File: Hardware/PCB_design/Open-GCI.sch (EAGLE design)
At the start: 29 parts, among them IC1 IC1, IC2 IC2, X1 USB

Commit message: Updated the schematics
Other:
- note added: "1.0"
- note added: "https://github.com/milador/Open-GCI"
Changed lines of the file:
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@@
 <part name="P+9" library="supply2" library_urn="urn:adsk.eagle:library:372" deviceset="+5V/2" device=""/>
 <part name="JP1" library="pinhead" library_urn="urn:adsk.eagle:library:325" deviceset="PINHD-1X2" device="" package3d_urn="urn:adsk.eagle:package:22435/2" value="No Rpi"/>
+<part name="FRAME1" library="frames" library_urn="urn:adsk.eagle:library:229" deviceset="FRAME_C_L" device="" value="https://github.com/milador/Open-GCI"/>
 </parts>
 <sheets>
 <sheet>
 <plain>
+<text x="270.51" y="-149.86" size="2.54" layer="94">https://github.com/milador/Open-GCI</text>
+<text x="360.68" y="-149.86" size="2.54" layer="94">1.0</text>
 </plain>
 <instances>
@@
 <instance part="P+9" gate="G$1" x="196.85" y="36.83"/>
 <instance part="JP1" gate="G$1" x="186.69" y="22.86" rot="R270"/>
+<instance part="FRAME1" gate="G$1" x="-184.15" y="-157.48" smashed="yes"/>
+<instance part="FRAME1" gate="G$2" x="267.97" y="-157.48"/>
 </instances>
 <busses>

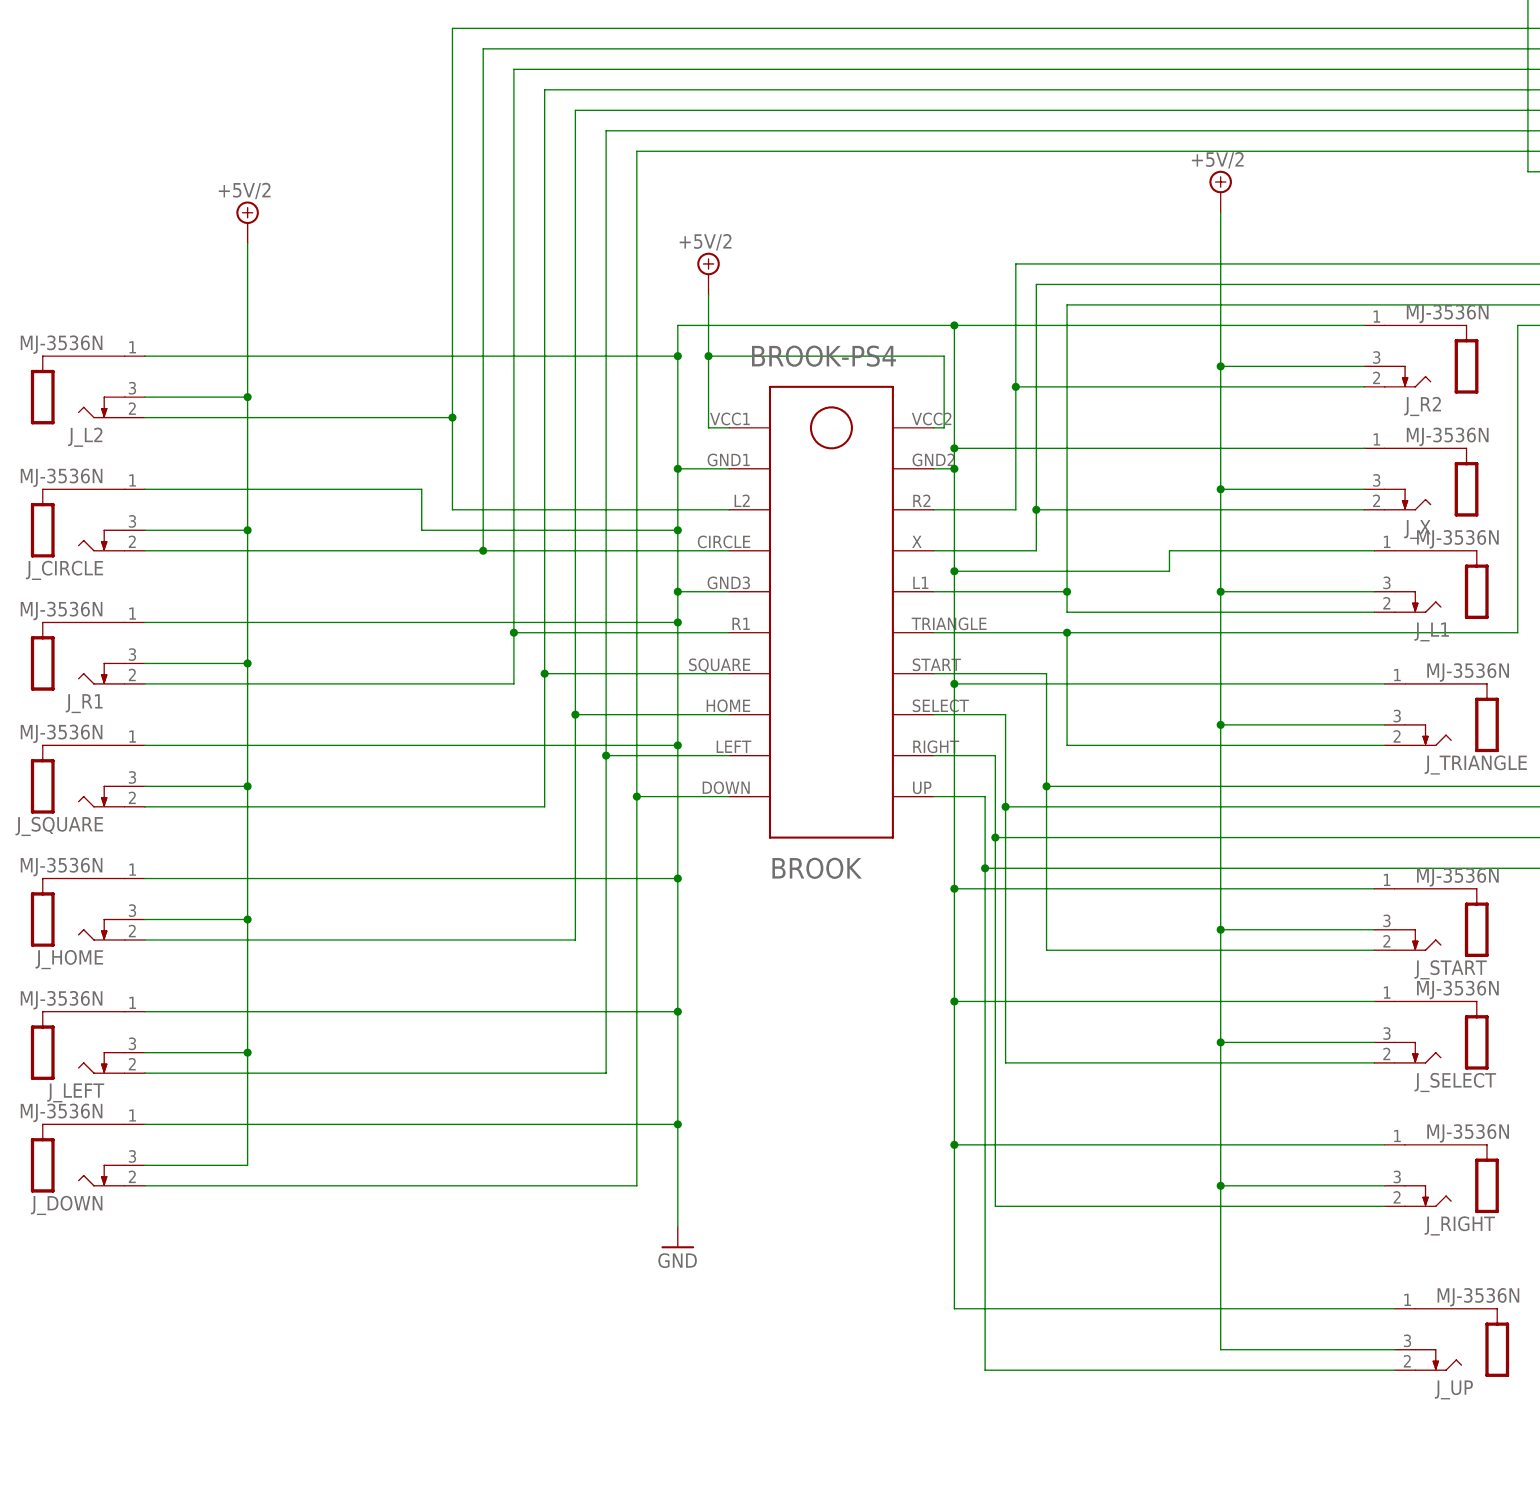
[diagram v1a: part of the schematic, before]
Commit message: Fixed the 3.5mm jack issue
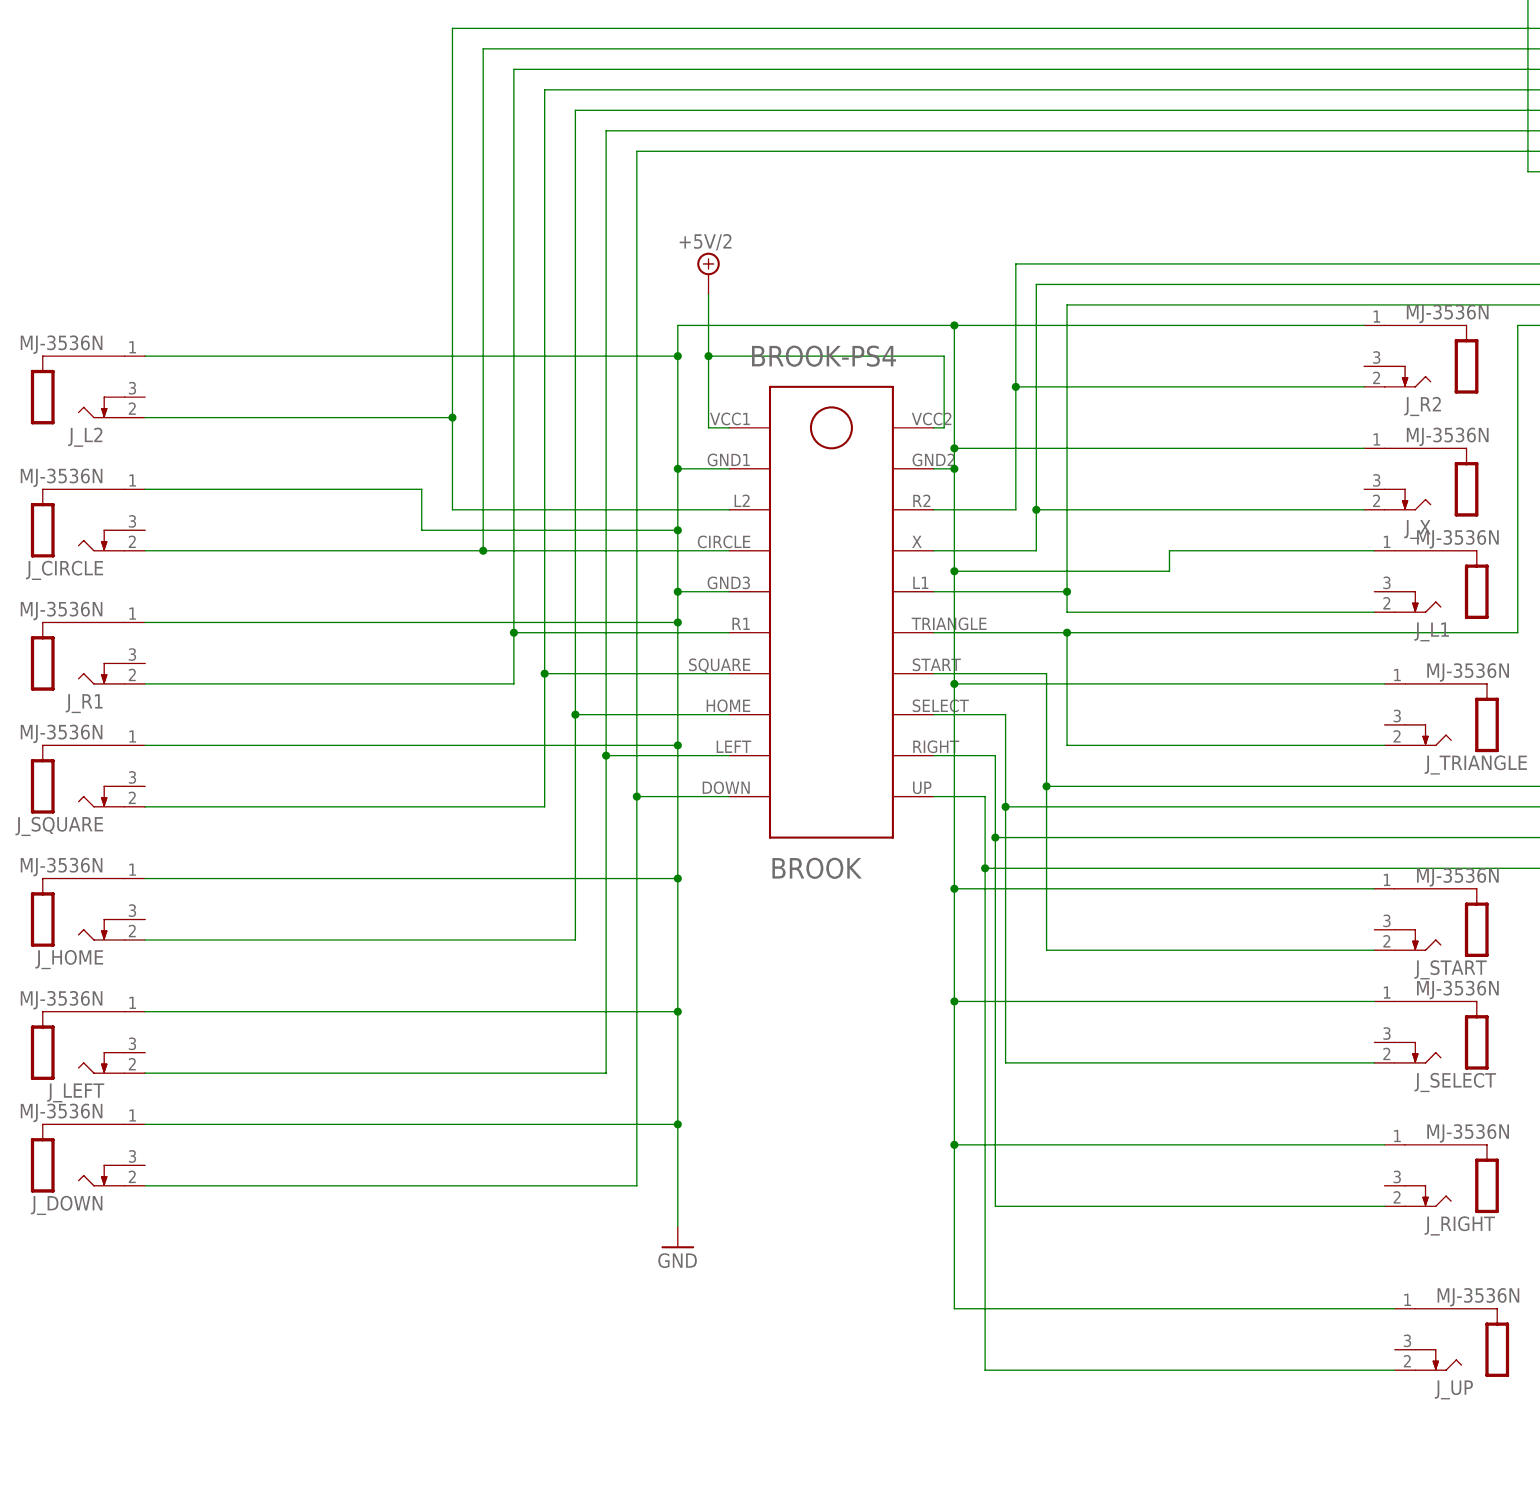
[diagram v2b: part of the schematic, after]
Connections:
- net +5V/2: no longer J_CIRCLE.TS, J_DOWN.TS, J_HOME.TS, J_L1.TS, J_L2.TS, J_LEFT.TS, J_R1.TS, J_R2.TS, J_RIGHT.TS, J_SELECT.TS, J_SQUARE.TS, J_START.TS, J_TRIANGLE.TS, J_UP.TS, J_X.TS
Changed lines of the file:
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@@
 <part name="P+2" library="supply2" library_urn="urn:adsk.eagle:library:372" deviceset="+5V/2" device=""/>
 <part name="P+6" library="supply2" library_urn="urn:adsk.eagle:library:372" deviceset="+5V/2" device=""/>
-<part name="P+1" library="supply2" library_urn="urn:adsk.eagle:library:372" deviceset="+5V/2" device=""/>
-<part name="P+7" library="supply2" library_urn="urn:adsk.eagle:library:372" deviceset="+5V/2" device=""/>
 <part name="R1" library="rcl" library_urn="urn:adsk.eagle:library:334" deviceset="R-US_" device="0204/7" package3d_urn="urn:adsk.eagle:package:23498/1" value="470"/>
 <part name="GND5" library="supply1" library_urn="urn:adsk.eagle:library:371" deviceset="GND" device=""/>
@@
 <instance part="P+2" gate="G$1" x="287.02" y="166.37"/>
 <instance part="P+6" gate="G$1" x="3.81" y="114.3"/>
-<instance part="P+1" gate="G$1" x="67.31" y="124.46"/>
-<instance part="P+7" gate="G$1" x="-53.34" y="120.65"/>
 <instance part="R1" gate="G$1" x="115.57" y="127"/>
 <instance part="GND5" gate="1" x="222.25" y="-90.17"/>
@@
 <junction x="0" y="90.17"/>
 <pinref part="J_L2" gate="G$1" pin="S"/>
-<wire x1="-66.04" y1="104.14" x2="0" y2="104.14" width="0.1524" layer="91"/>
 <junction x="0" y="104.14"/>
 <pinref part="J_R1" gate="G$1" pin="S"/>
 <junction x="0" y="71.12"/>
+<wire x1="-66.04" y1="104.14" x2="0" y2="104.14" width="0.1524" layer="91"/>
+<pinref part="J_CIRCLE" gate="G$1" pin="S"/>
 <wire x1="-66.04" y1="71.12" x2="0" y2="71.12" width="0.1524" layer="91"/>
-<pinref part="J_CIRCLE" gate="G$1" pin="S"/>
 <wire x1="-31.75" y1="82.55" x2="0" y2="82.55" width="0.1524" layer="91"/>
 <wire x1="-66.04" y1="87.63" x2="-31.75" y2="87.63" width="0.1524" layer="91"/>
@@
 <pinref part="J_SQUARE" gate="G$1" pin="S"/>
 <junction x="0" y="55.88"/>
+<pinref part="J_HOME" gate="G$1" pin="S"/>
 <wire x1="-66.04" y1="55.88" x2="0" y2="55.88" width="0.1524" layer="91"/>
-<pinref part="J_HOME" gate="G$1" pin="S"/>
-<wire x1="-66.04" y1="39.37" x2="0" y2="39.37" width="0.1524" layer="91"/>
 <junction x="0" y="39.37"/>
 <pinref part="J_LEFT" gate="G$1" pin="S"/>
 <junction x="0" y="22.86"/>
-<wire x1="-66.04" y1="22.86" x2="0" y2="22.86" width="0.1524" layer="91"/>
+<wire x1="-66.04" y1="39.37" x2="0" y2="39.37" width="0.1524" layer="91"/>
 <pinref part="J_DOWN" gate="G$1" pin="S"/>
 <junction x="0" y="8.89"/>
+<wire x1="-66.04" y1="22.86" x2="0" y2="22.86" width="0.1524" layer="91"/>
+<pinref part="J_R2" gate="G$1" pin="S"/>
 <wire x1="-66.04" y1="8.89" x2="0" y2="8.89" width="0.1524" layer="91"/>
-<pinref part="J_R2" gate="G$1" pin="S"/>
+<junction x="34.29" y="107.95"/>
 <wire x1="85.09" y1="107.95" x2="34.29" y2="107.95" width="0.1524" layer="91"/>
-<junction x="34.29" y="107.95"/>
 <wire x1="34.29" y1="90.17" x2="34.29" y2="77.47" width="0.1524" layer="91"/>
 <wire x1="34.29" y1="77.47" x2="34.29" y2="63.5" width="0.1524" layer="91"/>
@@
 <junction x="34.29" y="90.17"/>
 <pinref part="J_SELECT" gate="G$1" pin="S"/>
+<pinref part="J_START" gate="G$1" pin="S"/>
 <wire x1="87.63" y1="6.35" x2="34.29" y2="6.35" width="0.1524" layer="91"/>
-<pinref part="J_START" gate="G$1" pin="S"/>
+<pinref part="J_TRIANGLE" gate="G$1" pin="S"/>
 <wire x1="86.36" y1="24.13" x2="34.29" y2="24.13" width="0.1524" layer="91"/>
-<pinref part="J_TRIANGLE" gate="G$1" pin="S"/>
-<wire x1="86.36" y1="38.1" x2="34.29" y2="38.1" width="0.1524" layer="91"/>
 <junction x="34.29" y="63.5"/>
 <pinref part="J_L1" gate="G$1" pin="S"/>
+<wire x1="86.36" y1="38.1" x2="34.29" y2="38.1" width="0.1524" layer="91"/>
 <wire x1="87.63" y1="63.5" x2="34.29" y2="63.5" width="0.1524" layer="91"/>
 <wire x1="86.36" y1="80.01" x2="60.96" y2="80.01" width="0.1524" layer="91"/>
@@
 <wire x1="60.96" y1="77.47" x2="34.29" y2="77.47" width="0.1524" layer="91"/>
 <junction x="34.29" y="92.71"/>
-<wire x1="85.09" y1="92.71" x2="34.29" y2="92.71" width="0.1524" layer="91"/>
 <pinref part="U$2" gate="G$1" pin="GND3"/>
 <pinref part="U$2" gate="G$1" pin="GND1"/>
@@
 <junction x="34.29" y="24.13"/>
 <junction x="34.29" y="6.35"/>
+<wire x1="85.09" y1="92.71" x2="34.29" y2="92.71" width="0.1524" layer="91"/>
 </segment>
 <segment>
@@
 </segment>
 <segment>
-<wire x1="-53.34" y1="118.11" x2="-53.34" y2="99.06" width="0.1524" layer="91"/>
-<pinref part="J_DOWN" gate="G$1" pin="TS"/>
-<wire x1="-53.34" y1="99.06" x2="-53.34" y2="82.55" width="0.1524" layer="91"/>
-<wire x1="-53.34" y1="82.55" x2="-53.34" y2="66.04" width="0.1524" layer="91"/>
-<wire x1="-53.34" y1="66.04" x2="-53.34" y2="50.8" width="0.1524" layer="91"/>
-<wire x1="-53.34" y1="50.8" x2="-53.34" y2="34.29" width="0.1524" layer="91"/>
-<wire x1="-53.34" y1="34.29" x2="-53.34" y2="17.78" width="0.1524" layer="91"/>
-<wire x1="-53.34" y1="17.78" x2="-53.34" y2="3.81" width="0.1524" layer="91"/>
-<wire x1="-53.34" y1="3.81" x2="-66.04" y2="3.81" width="0.1524" layer="91"/>
-<pinref part="P+7" gate="G$1" pin="+5V/2"/>
-<pinref part="J_LEFT" gate="G$1" pin="TS"/>
-<wire x1="-66.04" y1="17.78" x2="-53.34" y2="17.78" width="0.1524" layer="91"/>
-<pinref part="J_HOME" gate="G$1" pin="TS"/>
-<wire x1="-66.04" y1="34.29" x2="-53.34" y2="34.29" width="0.1524" layer="91"/>
-<pinref part="J_L2" gate="G$1" pin="TS"/>
-<wire x1="-66.04" y1="99.06" x2="-53.34" y2="99.06" width="0.1524" layer="91"/>
-<pinref part="J_CIRCLE" gate="G$1" pin="TS"/>
-<wire x1="-66.04" y1="82.55" x2="-53.34" y2="82.55" width="0.1524" layer="91"/>
-<wire x1="-66.04" y1="66.04" x2="-53.34" y2="66.04" width="0.1524" layer="91"/>
-<pinref part="J_SQUARE" gate="G$1" pin="TS"/>
-<wire x1="-66.04" y1="50.8" x2="-53.34" y2="50.8" width="0.1524" layer="91"/>
-<junction x="-53.34" y="99.06"/>
-<junction x="-53.34" y="82.55"/>
-<junction x="-53.34" y="66.04"/>
-<junction x="-53.34" y="50.8"/>
-<junction x="-53.34" y="34.29"/>
-<junction x="-53.34" y="17.78"/>
-<pinref part="J_R1" gate="G$1" pin="TS"/>
-</segment>
-<segment>
-<pinref part="P+1" gate="G$1" pin="+5V/2"/>
-<wire x1="67.31" y1="121.92" x2="67.31" y2="102.87" width="0.1524" layer="91"/>
-<pinref part="J_R2" gate="G$1" pin="TS"/>
-<wire x1="85.09" y1="102.87" x2="67.31" y2="102.87" width="0.1524" layer="91"/>
-<wire x1="85.09" y1="87.63" x2="67.31" y2="87.63" width="0.1524" layer="91"/>
-<pinref part="J_L1" gate="G$1" pin="TS"/>
-<wire x1="67.31" y1="87.63" x2="67.31" y2="102.87" width="0.1524" layer="91"/>
-<wire x1="86.36" y1="74.93" x2="67.31" y2="74.93" width="0.1524" layer="91"/>
-<wire x1="67.31" y1="74.93" x2="67.31" y2="87.63" width="0.1524" layer="91"/>
-<pinref part="J_TRIANGLE" gate="G$1" pin="TS"/>
-<wire x1="87.63" y1="58.42" x2="67.31" y2="58.42" width="0.1524" layer="91"/>
-<wire x1="67.31" y1="58.42" x2="67.31" y2="74.93" width="0.1524" layer="91"/>
-<wire x1="86.36" y1="33.02" x2="67.31" y2="33.02" width="0.1524" layer="91"/>
-<wire x1="67.31" y1="33.02" x2="67.31" y2="58.42" width="0.1524" layer="91"/>
-<pinref part="J_SELECT" gate="G$1" pin="TS"/>
-<wire x1="86.36" y1="19.05" x2="67.31" y2="19.05" width="0.1524" layer="91"/>
-<wire x1="67.31" y1="19.05" x2="67.31" y2="33.02" width="0.1524" layer="91"/>
-<pinref part="J_RIGHT" gate="G$1" pin="TS"/>
-<wire x1="87.63" y1="1.27" x2="67.31" y2="1.27" width="0.1524" layer="91"/>
-<wire x1="67.31" y1="1.27" x2="67.31" y2="19.05" width="0.1524" layer="91"/>
-<wire x1="88.9" y1="-19.05" x2="67.31" y2="-19.05" width="0.1524" layer="91"/>
-<wire x1="67.31" y1="-19.05" x2="67.31" y2="1.27" width="0.1524" layer="91"/>
-<junction x="67.31" y="102.87"/>
-<junction x="67.31" y="87.63"/>
-<junction x="67.31" y="74.93"/>
-<junction x="67.31" y="58.42"/>
-<junction x="67.31" y="33.02"/>
-<junction x="67.31" y="19.05"/>
-<junction x="67.31" y="1.27"/>
-<pinref part="J_X" gate="G$1" pin="TS"/>
-<pinref part="J_START" gate="G$1" pin="TS"/>
-<pinref part="J_UP" gate="G$1" pin="TS"/>
-</segment>
-<segment>

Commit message: Updated PCB, Component listand gerber files
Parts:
- removed D1: RGB LED, open-gci-package:NEOPIXEL-RGB-THRUDIFFUSE
- removed U$1: RPI-ZERO, open-gci-package:RPI-ZERO
- removed U$2: BROOK, open-gci-package:BROOK
- removed X1: USB, open-gci-package:PN87520-S
- added H5, H6, H7, H8: STAND-OFF, SparkFun-Hardware:STAND-OFF
- added JP2: RASPBERRYPI ZERO, milador:RASPBERRYPI_ZERO
- added JP3: BROOK, milador:BROOK_2X10_FEMALE
- added L1: NEOPIXELS, milador:NEOPIXELS-5MM
- IC1: value IC1 -> SN74HCT245; device open-gci-package:74HCT245 -> milador:74HCT245N
- IC2: value IC2 -> SN74HCT245; device open-gci-package:74HCT245 -> milador:74HCT245N
- J_CIRCLE, J_DOWN, J_HOME, J_L1, J_L2, J_LEFT, J_R1, J_R2, J_RIGHT, J_SELECT, J_SQUARE, J_START, J_TRIANGLE, J_UP, J_X: value MJ-3536N -> SJ1-3535NG; device con-cuistack:MJ-3536N -> milador:SJ1-3535NG
- R1: device rcl:R-US_0204/7 -> milador:R-US_0204/7
- RN1, RN2: device resistor-sil:G08R -> milador:SIL9
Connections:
- removed net N$1: IC1.A0, J_L2.T, U$2.L2
- removed net N$10: IC2.A2, J_L1.T, U$2.L1
- removed net N$11: IC2.A3, J_TRIANGLE.T, U$2.TRIANGLE
- removed net N$12: IC2.A4, J_START.T, U$2.START
- removed net N$13: IC2.A5, J_SELECT.T, U$2.SELECT
- removed net N$14: IC2.A6, J_RIGHT.T, U$2.RIGHT
- removed net N$15: IC2.A7, J_UP.T, U$2.UP
- removed net N$16: IC1.B0, RN1.2, U$1.GPIO4/GCKL
- removed net N$17: IC1.B1, RN1.3, U$1.GPIO17/GEN0
- removed net N$18: IC1.B2, RN1.4, U$1.GPIO27/GEN2
- removed net N$19: IC1.B3, RN1.5, U$1.GPIO22/GEN3
- removed net N$2: IC1.A1, J_CIRCLE.T, U$2.CIRCLE
- removed net N$20: IC1.B5, RN1.7, U$1.GPIO9/MISO
- removed net N$21: IC1.B4, RN1.6, U$1.GPIO10/MOSI
- removed net N$22: IC1.B6, RN1.8, U$1.GPIO11/SCLK
- removed net N$23: IC1.B7, U$1.GPIO18
- removed net N$24: IC2.B1, RN2.3, U$1.GPIO13
- removed net N$25: IC2.B0, RN2.2, U$1.GPIO6
- removed net N$26: IC2.B2, RN2.4, U$1.GPIO19
- removed net N$27: IC2.B3, RN2.5, U$1.GPIO26
- removed net N$28: IC2.B4, RN2.6, U$1.GPIO21
- removed net N$29: IC2.B5, RN2.7, U$1.GPIO20
- removed net N$3: IC1.A2, J_R1.T, U$2.R1
- removed net N$30: IC2.B6, RN2.8, U$1.GPIO16
- removed net N$31: IC2.B7, RN2.9, U$1.GPIO12
- removed net N$4: IC1.A3, J_SQUARE.T, U$2.SQUARE
- removed net N$5: IC1.A4, J_HOME.T, U$2.HOME
- removed net N$6: IC1.A5, J_LEFT.T, U$2.LEFT
- removed net N$7: IC1.A6, J_DOWN.T, U$2.DOWN
- removed net N$8: IC2.A0, J_R2.T, U$2.R2
- removed net N$9: IC2.A1, J_X.T, U$2.X
- new net NGP11: IC1.17, JP2.GPIO17/GEN0, RN1.3
- new net NGP12: IC1.11, JP2.GPIO18
- new net NGP13: IC1.16, JP2.GPIO27/GEN2, RN1.4
- new net NGP15: IC1.15, JP2.GPIO22/GEN3, RN1.5
- new net NGP19: IC1.14, JP2.GPIO10/MOSI, RN1.6
- new net NGP21: IC1.13, JP2.GPIO9/MISO, RN1.7
- new net NGP23: IC1.12, JP2.GPIO11/SCLK, RN1.8
- new net NGP31: IC2.18, JP2.GPIO6, RN2.2
- new net NGP32: IC2.11, JP2.GPIO12, RN2.9
- new net NGP33: IC2.17, JP2.GPIO13, RN2.3
- new net NGP35: IC2.16, JP2.GPIO19, RN2.4
- new net NGP36: IC2.12, JP2.GPIO16, RN2.8
- new net NGP37: IC2.15, JP2.GPIO26, RN2.5
- new net NGP38: IC2.13, JP2.GPIO20, RN2.7
- new net NGP40: IC2.14, JP2.GPIO21, RN2.6
- new net NGP7: IC1.18, JP2.GPIO4/GCKL, RN1.2
- new net NJ_CIR: IC1.3, JP3.CIRCLE, J_CIRCLE.2
- new net NJ_DOWN: IC1.8, JP3.DOWN, J_DOWN.2
- new net NJ_HOME: IC1.6, JP3.HOME, J_HOME.2
- new net NJ_L1: IC2.4, JP3.L1, J_L1.2
- new net NJ_L2: IC1.2, JP3.L2, J_L2.2
- new net NJ_LEFT: IC1.7, JP3.LEFT, J_LEFT.2
- new net NJ_R1: IC1.4, JP3.R1, J_R1.2
- new net NJ_R2: IC2.2, JP3.R2, J_R2.2
- new net NJ_RIGHT: IC2.8, JP3.RIGHT, J_RIGHT.2
- new net NJ_SELECT: IC2.7, JP3.SELECT, J_SELECT.2
- new net NJ_SQU: IC1.5, JP3.SQUARE, J_SQUARE.2
- new net NJ_START: IC2.6, JP3.START, J_START.2
- new net NJ_TRI: IC2.5, JP3.TRIANGLE, J_TRIANGLE.2
- new net NJ_UP: IC2.9, JP3.UP, J_UP.2
- new net NJ_X: IC2.3, JP3.X, J_X.2
- net +3V3: now also JP2.+3V3@1, JP2.+3V3@2; no longer U$1.+3V3@1, U$1.+3V3@2
- net +5V: now also IC1.20, IC2.20, JP2.+5V@1, JP2.+5V@2, L1.VDD; no longer D1.5V, IC1.VCC, IC2.VCC, U$1.+5V@1, U$1.+5V@2
- net +5V/2: now also JP3.VCC1, JP3.VCC2; no longer U$2.VCC1, U$2.VCC2, X1.1
- net GND: now also IC1.1, IC1.10, IC1.19, IC2.1, IC2.10, IC2.19, JP2.GND@1, JP2.GND@2, JP2.GND@3, JP2.GND@4, JP2.GND@5, JP2.GND@6, JP2.GND@7, JP2.GND@8, JP3.GND1, JP3.GND2, JP3.GND3, J_CIRCLE.1, J_DOWN.1, J_HOME.1, J_L1.1, J_L2.1, J_LEFT.1, J_R1.1, J_R2.1, J_RIGHT.1, J_SELECT.1, J_SQUARE.1, J_START.1, J_TRIANGLE.1, J_UP.1, J_X.1, L1.DO, L1.VSS; no longer D1.DOUT, D1.GND, IC1.DIR, IC1.GND, IC1.OE, IC2.DIR, IC2.GND, IC2.OE, J_CIRCLE.S, J_DOWN.S, J_HOME.S, J_L1.S, J_L2.S, J_LEFT.S, J_R1.S, J_R2.S, J_RIGHT.S, J_SELECT.S, J_SQUARE.S, J_START.S, J_TRIANGLE.S, J_UP.S, J_X.S, U$1.GND@1, U$1.GND@2, U$1.GND@3, U$1.GND@4, U$1.GND@5, U$1.GND@6, U$1.GND@7, U$1.GND@8, U$2.GND1, U$2.GND2, U$2.GND3, X1.2, X1.3, X1.4, X1.S1, X1.S2
- net N$32: now also IC1.9; no longer IC1.A7
- net N$33: now also L1.DI; no longer D1.DIN
